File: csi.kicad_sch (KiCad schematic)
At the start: 5 parts, among them J6 WE_68715014022

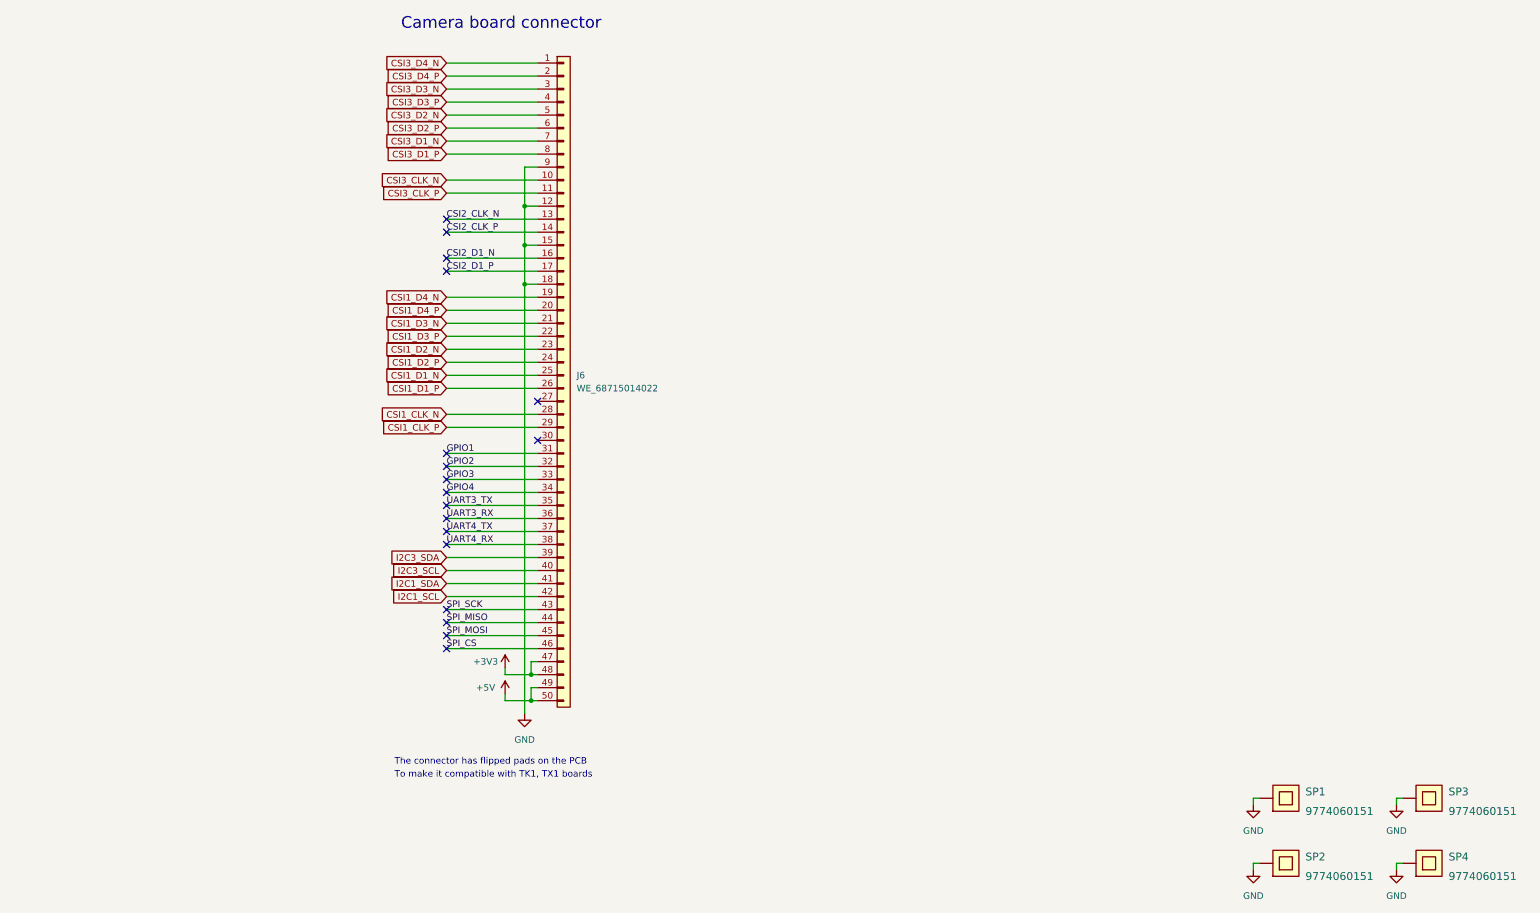
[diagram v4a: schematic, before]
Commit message: Introduce component standardization
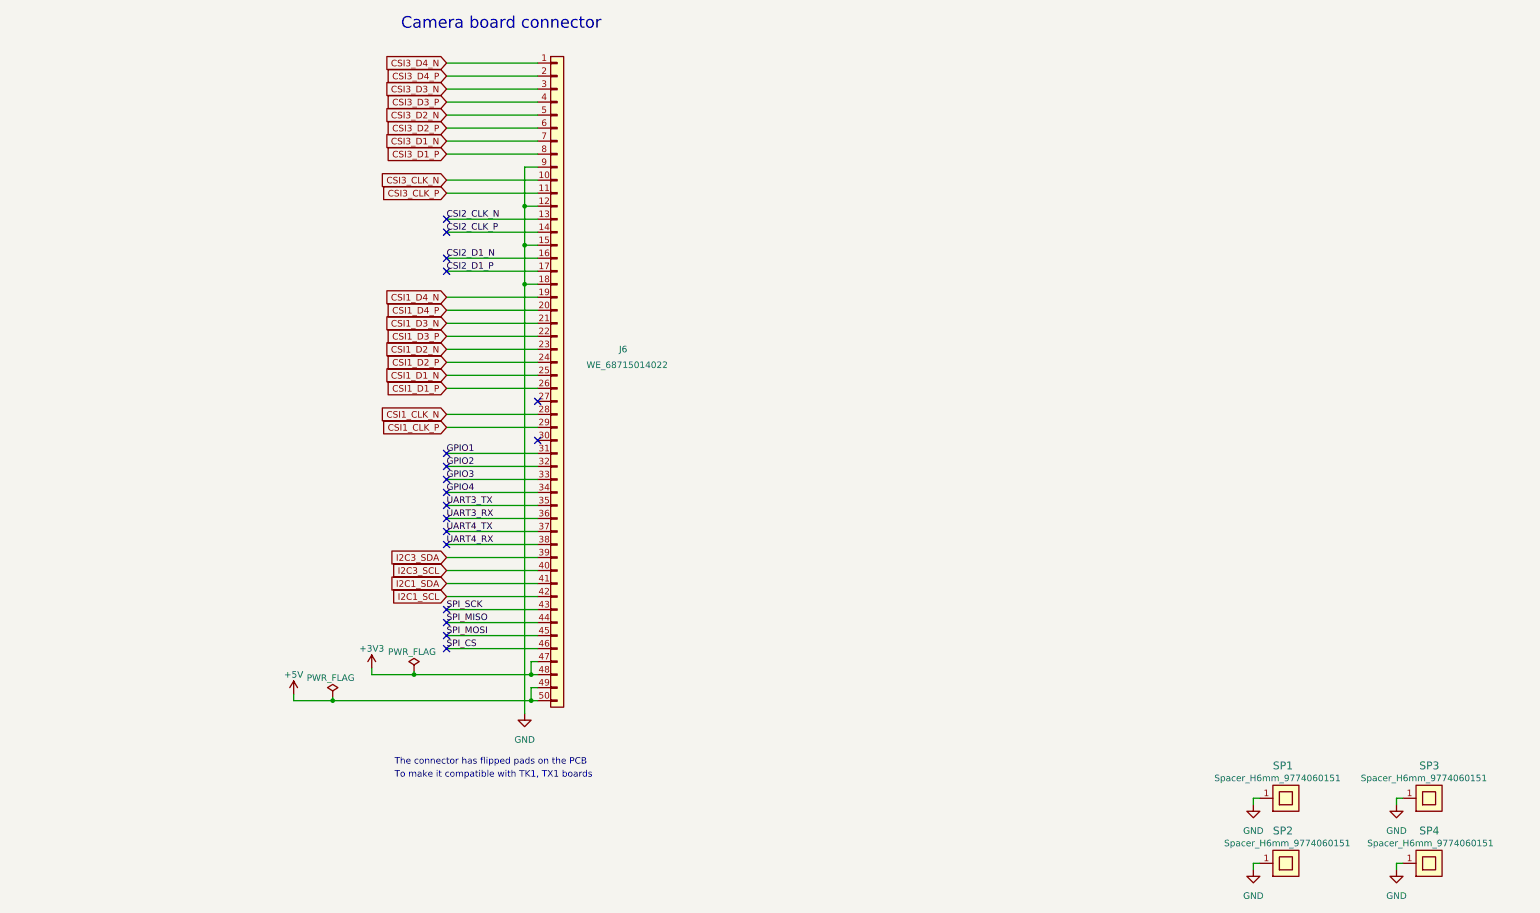
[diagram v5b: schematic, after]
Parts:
- J6: Author (none) -> Antmicro; License (none) -> Apache-2.0; Manufacturer Wurth Elektronik -> Würth Elektronik
- SP1, SP2, SP3, SP4: value 9774060151 -> Spacer_H6mm_9774060151; footprint antmicro-hdmi-mipi-bridge-hw-footprints:9774060151 -> antmicro-hdmi-mipi-bridge-hw-footprints:Spacer_SMD_M2.5_H6mm_Wurth_9774060151; symbol antmicro-hdmi-mipi-bridge-hw:9774060151 -> antmicro-hdmi-mipi-bridge-hw:Spacer_H6mm_9774060151; Author (none) -> Antmicro; License (none) -> Apache-2.0; Manufacturer Wurth Elektronik -> Würth Elektronik
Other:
- title: (none) -> HDMI-MIPI Bridge
